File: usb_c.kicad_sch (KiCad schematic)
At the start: 8 parts, among them J201 USB_C_Receptacle_USB2.0_16P, U102 USBLC6-2SC6

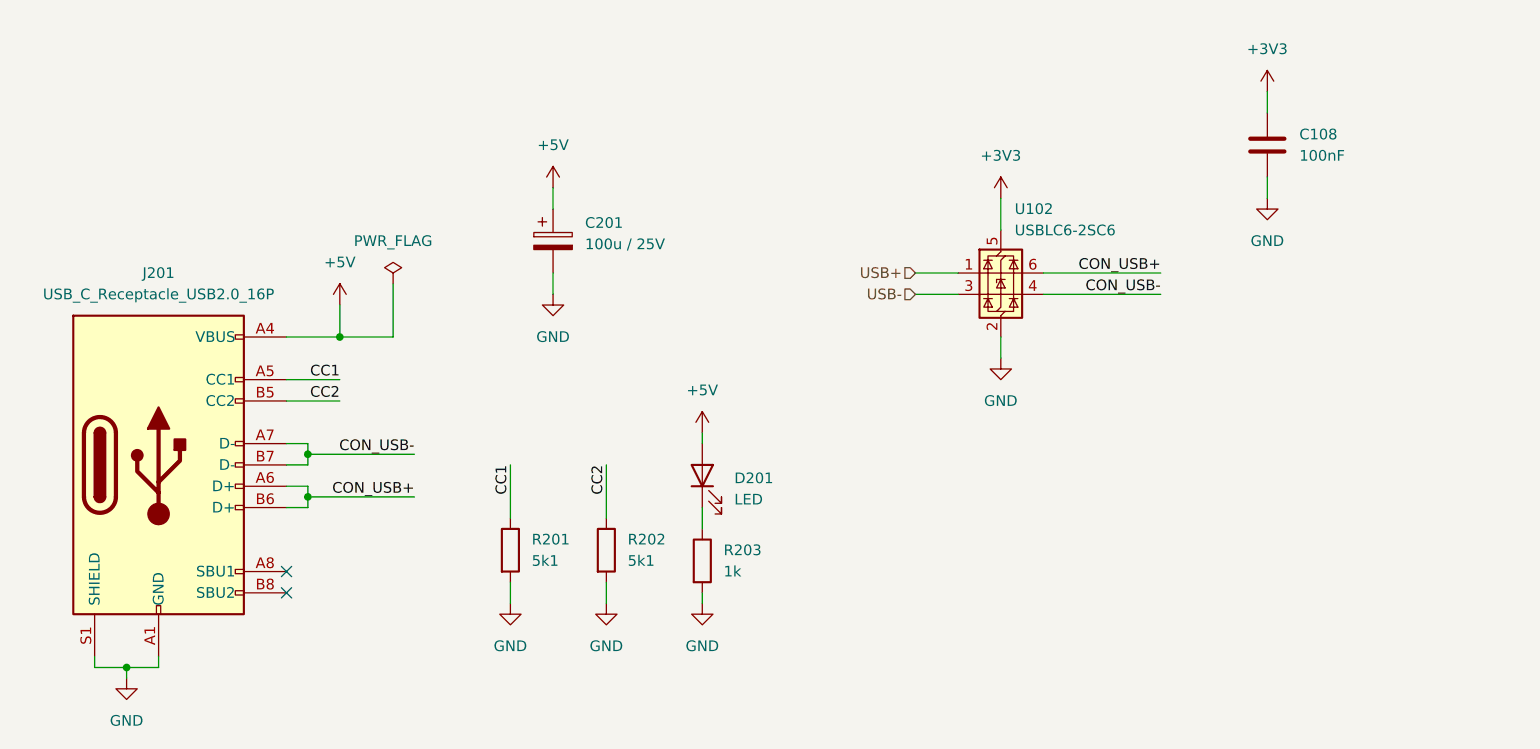
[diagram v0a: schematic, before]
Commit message: add basic structure, update readme
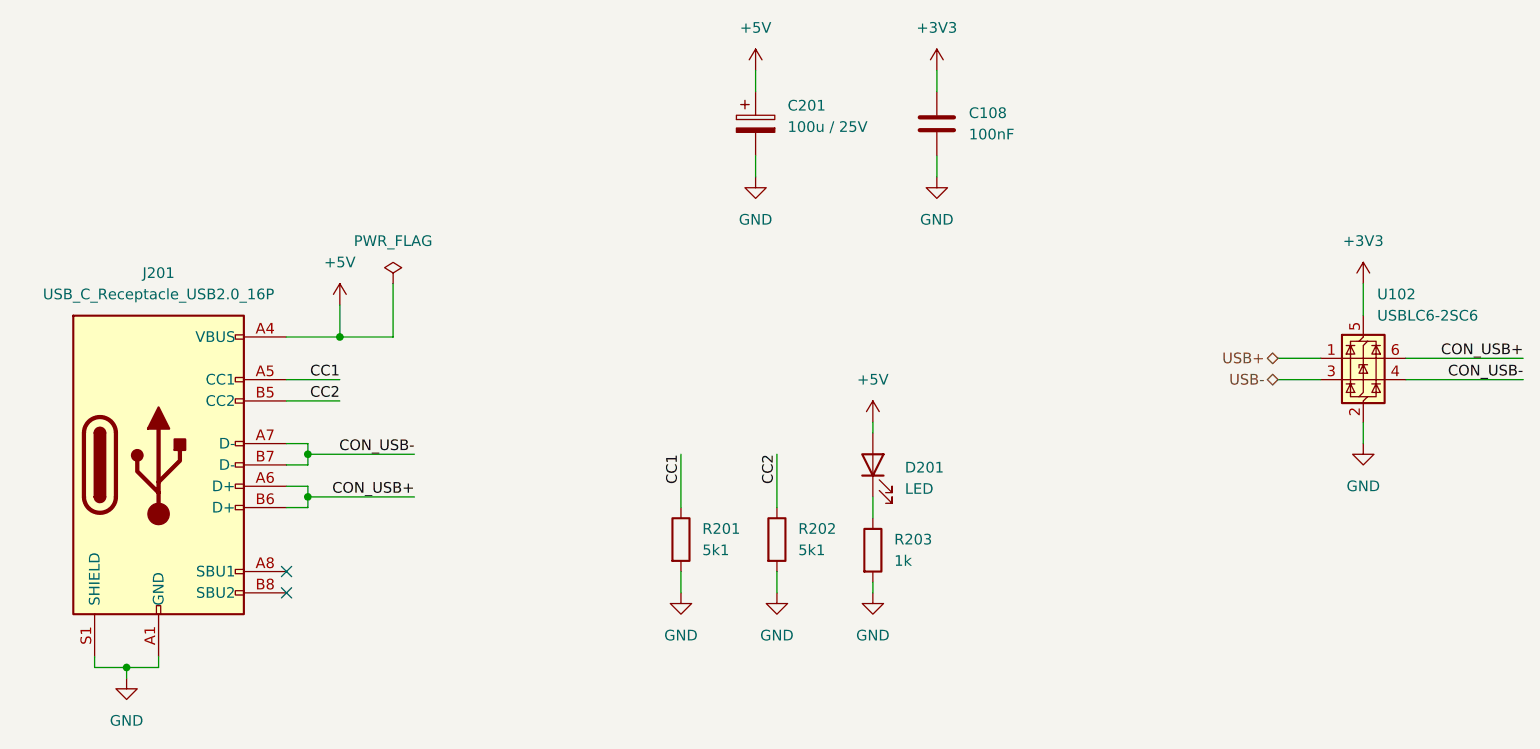
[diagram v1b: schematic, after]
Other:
- moved on the sheet: C108, C201, D201, R201, R202, R203, U102

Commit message: Update USB-C and USB-Hub Schematics with New Titles and Reference Changes
- Changed title from "DebugBoard" to "USB-C" in usb_c.kicad_sch.
- Changed title from "DebugBoard" to "USB-Hub" in usb_hub.kicad_sch.
- Updated multiple component references in usb_c.kicad_sch to new identifiers (#PWR0301 to #PWR0312, D301, U301, etc.).
- Updated component reference from "R103" to "R501" in usb_hub.kicad_sch.
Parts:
- renumbered C201 to C301, C108 to C302, D201 to D301, J201 to J301, R201 to R301, R202 to R302, R203 to R303, U102 to U301
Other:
- title: DebugBoard -> USB-C
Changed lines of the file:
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@@
 	(paper "A4")
 	(title_block
-		(title "DebugBoard")
+		(title "USB-C")
 		(rev "<<HASH>>")
 		(company "Amateurfunkclub für Remote Stationen")
@@
 		(dnp no)
 		(fields_autoplaced yes)
-		(property "Reference" "#PWR0216"
+		(property "Reference" "#PWR0305"
 			(at 133.35 77.47 0)
 			(effects
@@
 			(project "main"
 				(path "/f228839c-6576-40b2-ae70-679b7b460639/3e14524a-e89f-475c-8490-f5cddd2eec77"
-					(reference "#PWR0216")
+					(reference "#PWR0305")
 					(unit 1)
 				)
@@
 		(dnp no)
 		(fields_autoplaced yes)
-		(property "Reference" "#PWR0206"
+		(property "Reference" "#PWR0307"
 			(at 147.32 104.14 0)
 			(effects
@@
 			(project "main"
 				(path "/f228839c-6576-40b2-ae70-679b7b460639/3e14524a-e89f-475c-8490-f5cddd2eec77"
-					(reference "#PWR0206")
+					(reference "#PWR0307")
 					(unit 1)
 				)
@@
 		(on_board yes)
 		(dnp no)
-		(property "Reference" "#PWR0116"
+		(property "Reference" "#PWR0310"
 			(at 154.94 77.47 0)
 			(effects
@@
 			(project "main"
 				(path "/f228839c-6576-40b2-ae70-679b7b460639/3e14524a-e89f-475c-8490-f5cddd2eec77"
-					(reference "#PWR0116")
+					(reference "#PWR0310")
 					(unit 1)
 				)
@@
 		(dnp no)
 		(fields_autoplaced yes)
-		(property "Reference" "D201"
+		(property "Reference" "D301"
 			(at 151.13 105.7274 90)
 			(effects
@@
 			(project "main"
 				(path "/f228839c-6576-40b2-ae70-679b7b460639/3e14524a-e89f-475c-8490-f5cddd2eec77"
-					(reference "D201")
+					(reference "D301")
 					(unit 1)
 				)
@@
 		(dnp no)
 		(fields_autoplaced yes)
-		(property "Reference" "#PWR0207"
+		(property "Reference" "#PWR0308"
 			(at 147.32 127 0)
 			(effects
@@
 			(project "main"
 				(path "/f228839c-6576-40b2-ae70-679b7b460639/3e14524a-e89f-475c-8490-f5cddd2eec77"
-					(reference "#PWR0207")
+					(reference "#PWR0308")
 					(unit 1)
 				)
@@
 		(dnp no)
 		(fields_autoplaced yes)
-		(property "Reference" "#PWR0205"
+		(property "Reference" "#PWR0306"
 			(at 135.89 127 0)
 			(effects
@@
 			(project "main"
 				(path "/f228839c-6576-40b2-ae70-679b7b460639/3e14524a-e89f-475c-8490-f5cddd2eec77"
-					(reference "#PWR0205")
+					(reference "#PWR0306")
 					(unit 1)
 				)
@@
 		(on_board yes)
 		(dnp no)
-		(property "Reference" "#PWR0121"
+		(property "Reference" "#PWR0312"
 			(at 205.74 109.22 0)
 			(effects
@@
 			(project "main"
 				(path "/f228839c-6576-40b2-ae70-679b7b460639/3e14524a-e89f-475c-8490-f5cddd2eec77"
-					(reference "#PWR0121")
+					(reference "#PWR0312")
 					(unit 1)
 				)
@@
 		(dnp no)
 		(fields_autoplaced yes)
-		(property "Reference" "#PWR0201"
+		(property "Reference" "#PWR0301"
 			(at 58.42 137.16 0)
 			(effects
@@
 			(project "main"
 				(path "/f228839c-6576-40b2-ae70-679b7b460639/3e14524a-e89f-475c-8490-f5cddd2eec77"
-					(reference "#PWR0201")
+					(reference "#PWR0301")
 					(unit 1)
 				)
@@
 		(dnp no)
 		(fields_autoplaced yes)
-		(property "Reference" "#FLG0201"
+		(property "Reference" "#FLG0301"
 			(at 90.17 81.915 0)
 			(effects
@@
 			(project "main"
 				(path "/f228839c-6576-40b2-ae70-679b7b460639/3e14524a-e89f-475c-8490-f5cddd2eec77"
-					(reference "#FLG0201")
+					(reference "#FLG0301")
 					(unit 1)
 				)
@@
 		(on_board yes)
 		(dnp no)
-		(property "Reference" "U102"
+		(property "Reference" "U301"
 			(at 207.3911 85.09 0)
 			(effects
@@
 			(project "main"
 				(path "/f228839c-6576-40b2-ae70-679b7b460639/3e14524a-e89f-475c-8490-f5cddd2eec77"
-					(reference "U102")
+					(reference "U301")
 					(unit 1)
 				)
@@
 		(dnp no)
 		(fields_autoplaced yes)
-		(property "Reference" "#PWR0203"
+		(property "Reference" "#PWR0303"
 			(at 124.46 127 0)
 			(effects
@@
 			(project "main"
 				(path "/f228839c-6576-40b2-ae70-679b7b460639/3e14524a-e89f-475c-8490-f5cddd2eec77"
-					(reference "#PWR0203")
+					(reference "#PWR0303")
 					(unit 1)
 				)
@@
 		(dnp no)
 		(fields_autoplaced yes)
-		(property "Reference" "R201"
+		(property "Reference" "R301"
 			(at 127 113.0299 0)
 			(effects
@@
 			(project "main"
 				(path "/f228839c-6576-40b2-ae70-679b7b460639/3e14524a-e89f-475c-8490-f5cddd2eec77"
-					(reference "R201")
+					(reference "R301")
 					(unit 1)
 				)
@@
 		(dnp no)
 		(fields_autoplaced yes)
-		(property "Reference" "C201"
+		(property "Reference" "C301"
 			(at 137.16 62.6109 0)
 			(effects
@@
 			(project "main"
 				(path "/f228839c-6576-40b2-ae70-679b7b460639/3e14524a-e89f-475c-8490-f5cddd2eec77"
-					(reference "C201")
+					(reference "C301")
 					(unit 1)
 				)
@@
 		(dnp no)
 		(fields_autoplaced yes)
-		(property "Reference" "J201"
+		(property "Reference" "J301"
 			(at 62.23 82.55 0)
 			(effects
@@
 			(project "main"
 				(path "/f228839c-6576-40b2-ae70-679b7b460639/3e14524a-e89f-475c-8490-f5cddd2eec77"
-					(reference "J201")
+					(reference "J301")
 					(unit 1)
 				)
@@
 		(dnp no)
 		(fields_autoplaced yes)
-		(property "Reference" "#PWR0215"
+		(property "Reference" "#PWR0304"
 			(at 133.35 62.23 0)
 			(effects
@@
 			(project "main"
 				(path "/f228839c-6576-40b2-ae70-679b7b460639/3e14524a-e89f-475c-8490-f5cddd2eec77"
-					(reference "#PWR0215")
+					(reference "#PWR0304")
 					(unit 1)
 				)
@@
 		(dnp no)
 		(fields_autoplaced yes)
-		(property "Reference" "R202"
+		(property "Reference" "R302"
 			(at 138.43 113.0299 0)
 			(effects
@@
 			(project "main"
 				(path "/f228839c-6576-40b2-ae70-679b7b460639/3e14524a-e89f-475c-8490-f5cddd2eec77"
-					(reference "R202")
+					(reference "R302")
 					(unit 1)
 				)
@@
 		(on_board yes)
 		(dnp no)
-		(property "Reference" "C108"
+		(property "Reference" "C302"
 			(at 158.75 63.4999 0)
 			(effects
@@
 			(project "main"
 				(path "/f228839c-6576-40b2-ae70-679b7b460639/3e14524a-e89f-475c-8490-f5cddd2eec77"
-					(reference "C108")
+					(reference "C302")
 					(unit 1)
 				)
@@
 		(dnp no)
 		(fields_autoplaced yes)
-		(property "Reference" "R203"
+		(property "Reference" "R303"
 			(at 149.86 114.2999 0)
 			(effects
@@
 			(project "main"
 				(path "/f228839c-6576-40b2-ae70-679b7b460639/3e14524a-e89f-475c-8490-f5cddd2eec77"
-					(reference "R203")
+					(reference "R303")
 					(unit 1)
 				)
@@
 		(dnp no)
 		(fields_autoplaced yes)
-		(property "Reference" "#PWR0115"
+		(property "Reference" "#PWR0309"
 			(at 154.94 62.23 0)
 			(effects
@@
 			(project "main"
 				(path "/f228839c-6576-40b2-ae70-679b7b460639/3e14524a-e89f-475c-8490-f5cddd2eec77"
-					(reference "#PWR0115")
+					(reference "#PWR0309")
 					(unit 1)
 				)
@@
 		(dnp no)
 		(fields_autoplaced yes)
-		(property "Reference" "#PWR0120"
+		(property "Reference" "#PWR0311"
 			(at 205.74 87.63 0)
 			(effects
@@
 			(project "main"
 				(path "/f228839c-6576-40b2-ae70-679b7b460639/3e14524a-e89f-475c-8490-f5cddd2eec77"
-					(reference "#PWR0120")
+					(reference "#PWR0311")
 					(unit 1)
 				)
@@
 		(dnp no)
 		(fields_autoplaced yes)
-		(property "Reference" "#PWR0202"
+		(property "Reference" "#PWR0302"
 			(at 83.82 90.17 0)
 			(effects
@@
 			(project "main"
 				(path "/f228839c-6576-40b2-ae70-679b7b460639/3e14524a-e89f-475c-8490-f5cddd2eec77"
-					(reference "#PWR0202")
+					(reference "#PWR0302")
 					(unit 1)
 				)
